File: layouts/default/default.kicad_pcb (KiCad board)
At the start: 4 copper layers, 66 x 21 mm, 66 parts

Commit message: update layouts and add jlink base compact layout
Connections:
- net -line renamed TARGET_SWCLK
- net GND_DETECT renamed TARGET_GND_DETECT
- net SWDIO renamed TARGET_SWDIO
- net SWO renamed TARGET_SWO
- net UART_RX renamed TARGET_UART_RX
- net UART_TX renamed TARGET_UART_TX
- net nRESET renamed TARGET_RESET
- U8 pad 19: TESTEN -> GND
- USB1 pad : (no net) -> usb_connector.connector.package.footprint.pins[0].net-net

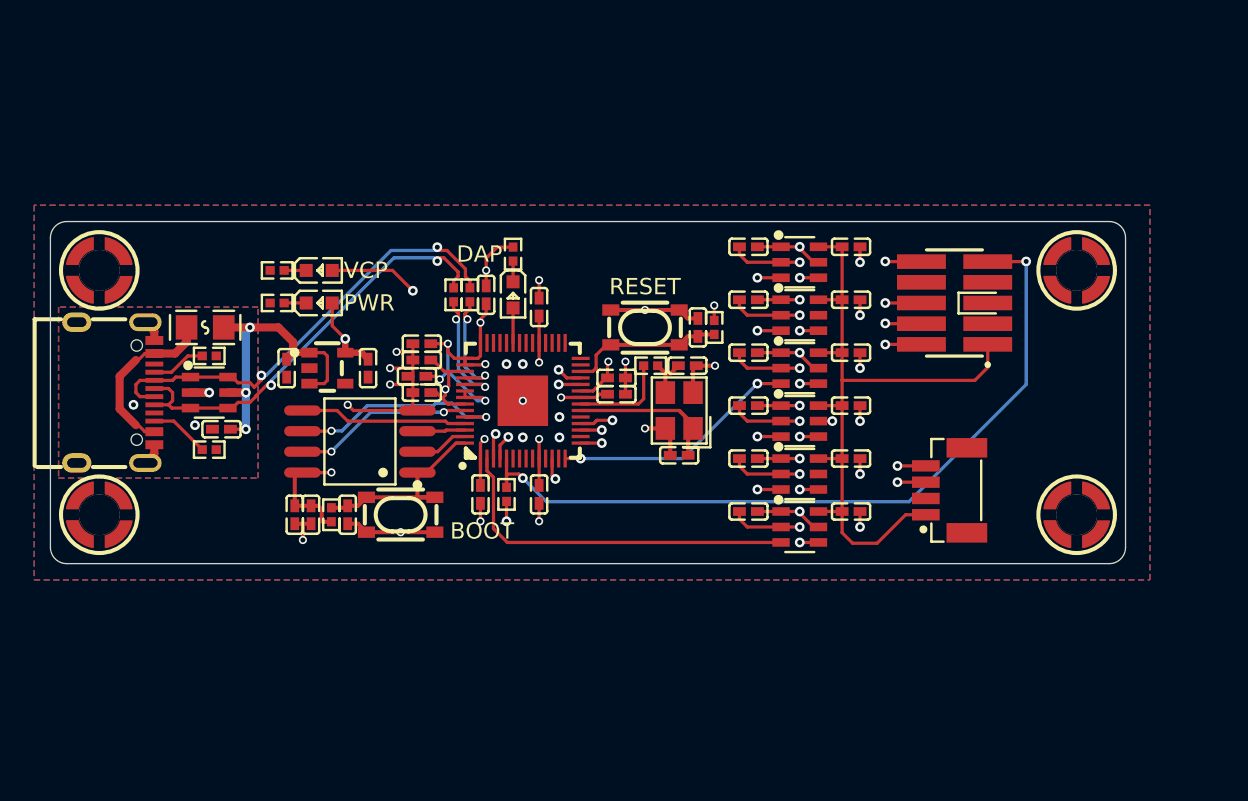
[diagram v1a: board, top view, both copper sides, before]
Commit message: refactor jlink connector, make stick prety
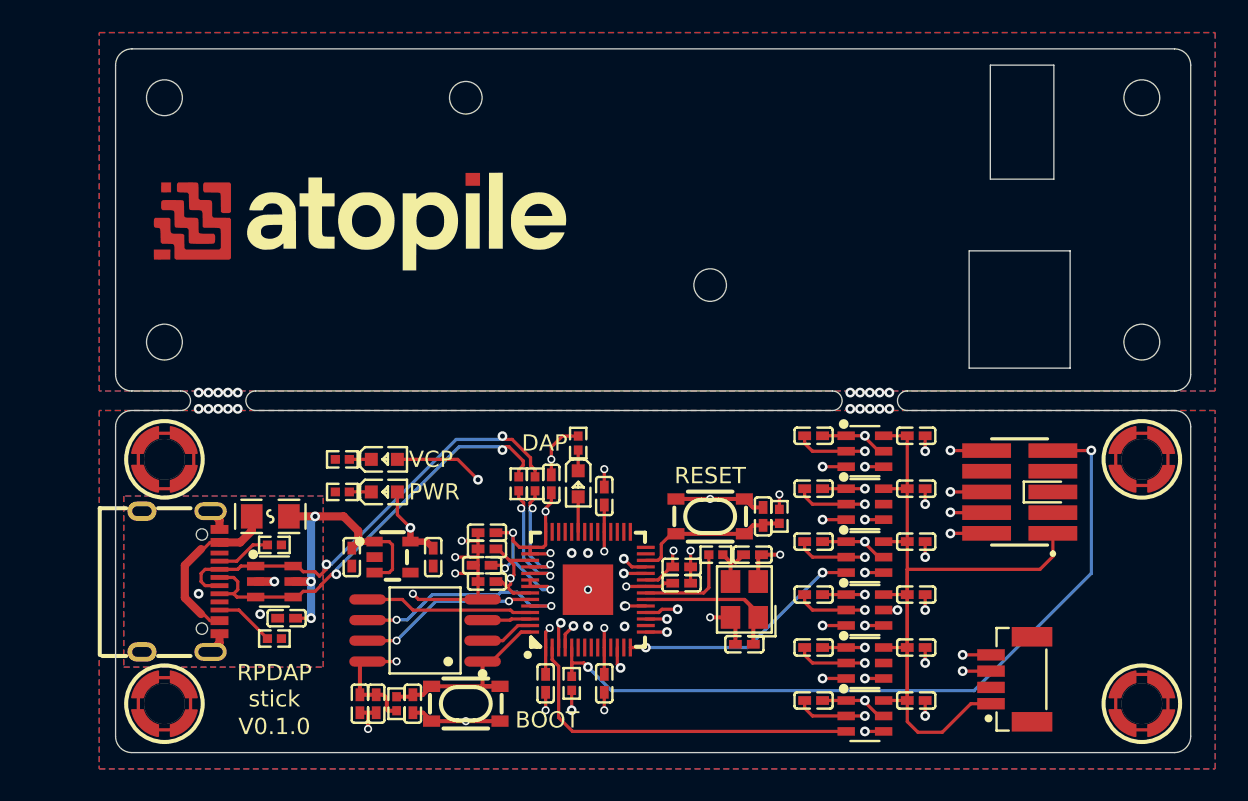
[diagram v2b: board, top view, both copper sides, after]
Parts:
- added LOGO1: , atopile_Logo_25x6mm:atopile_Logo_25x6mm, F.Cu at (15.0, -11.0)
- moved C13 12.3 mm to (42.9, 15.2)
- moved C15 12.3 mm to (18.3, 18.6)
- moved C17 12.3 mm to (22.8, 11.1)
- moved C26 12.3 mm to (26.4, 17.4)
- moved C27 12.3 mm to (30.0, 17.4)
- moved C28 12.3 mm to (15.0, 18.6)
- moved C29 12.3 mm to (16.0, 18.6)
- moved C5 12.3 mm to (42.9, 8.65)
- moved C7 12.3 mm to (42.9, 5.40)
- moved F1 12.3 mm to (9.50, 7.10)
- moved R1 12.3 mm to (28.0, 17.4)
- moved R2 12.3 mm to (17.2, 18.6)
- moved SW1 12.3 mm to (21.5, 18.6)
- moved U10 12.3 mm to (55.0, 17.1)
- moved U12 12.3 mm to (3.00, 18.6)
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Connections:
- net -hv renamed power_b-VCC
- net DVDD renamed _core_power-VCC
- net QSPI_SCLK renamed clock
- net QSPI_SS renamed chip_select
- net SWCLK renamed SWD_CLK
- net SWD renamed SWD_DIO
- net cathode-0 renamed power_indicator-cathode
- net cathode-1 renamed vcp_indicator-cathode
- net debug_connector-line renamed TDI
- net hv renamed power_vbus-VCC
- net line-0 renamed cc[0]-line
- net line-1 renamed cc[1]-line
- net line-2 renamed sbu[0]-line
- net line-3 renamed sbu[1]-line
- net rpdap-line-0 renamed model-a-line
- net rpdap-line-1 renamed gpio[9]-line
- net rpdap-line-2 renamed level_shifter[1]-a-line
- net rpdap-line-3 renamed level_shifter[2]-a-line
- net rpdap-line-4 renamed level_shifter[3]-a-line
- net rpdap-line-5 renamed TX
- net rpdap-line-6 renamed RX
- net rpdap.ldo.ldo.package.footprint.pins[3].net-net renamed rpdap-net
- net rpdap.mcu-line-0 renamed gpio[26]-line
- net rpdap.mcu-line-1 renamed gpio[27]-line
- net rpdap.mcu-line-2 renamed gpio[28]-line
- net rpdap.mcu-line-3 renamed analog[3]-line
- net rpdap.mcu-line-4 renamed SCLK
- net rpdap.mcu-line-5 renamed MOSI
- net rpdap.mcu-line-6 renamed MISO
- net standoff[0].footprint.pins[0].net-net renamed standoff[0]-net
- net standoff[1].footprint.pins[0].net-net renamed standoff[1]-net
- net standoff[2].footprint.pins[0].net-net renamed standoff[2]-net
- net standoff[3].footprint.pins[0].net-net renamed standoff[3]-net
- net xin renamed XIN
- net xout renamed XOUT
- U3 pad 5: (no net) -> 3V3
- U4 pad 5: (no net) -> GND
- U5 pad 5: (no net) -> 3V3
- U6 pad 5: (no net) -> 3V3
- U7 pad 5: (no net) -> GND
- USB1 pad : usb_connector.connector.package.footprint.pins[0].net-net -> (no net)
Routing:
- net GND: track 76.3 -> 121.3 mm, vias 32 -> 33
- net power_b-VCC: track 43.1 -> 51.1 mm
- net (no net): vias 2 -> 22
- added copper zone on In2.Cu, net GND
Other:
- board size 66 x 21 mm -> 66 x 43.2 mm
- board text added: "DET - GND GND Vrev"
- board text added: "RPDAP"
- board text added: "RPDAP stick"
- board text added: "RST - SWO CLK DIO"
- board text added: "RX TX GND Vref"
- board text added: "STICK"
- board text added: "V0.1.0"
- board text added: "VCP PWR"
